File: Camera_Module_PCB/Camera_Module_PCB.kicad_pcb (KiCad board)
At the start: 4 copper layers, 111 parts, among them J1 SS-52400-002, J2 Conn_01x02, J3 FFC2A32-24-T, J4 U.FL-R-SMT-1_80_, SW1 SW_DIP_x01, SW2 SW_Push, SW3 SW_Push, U2 ESP32-S3R8, U4 MAX98357AETE_T, U5 AP3032KTR-G1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

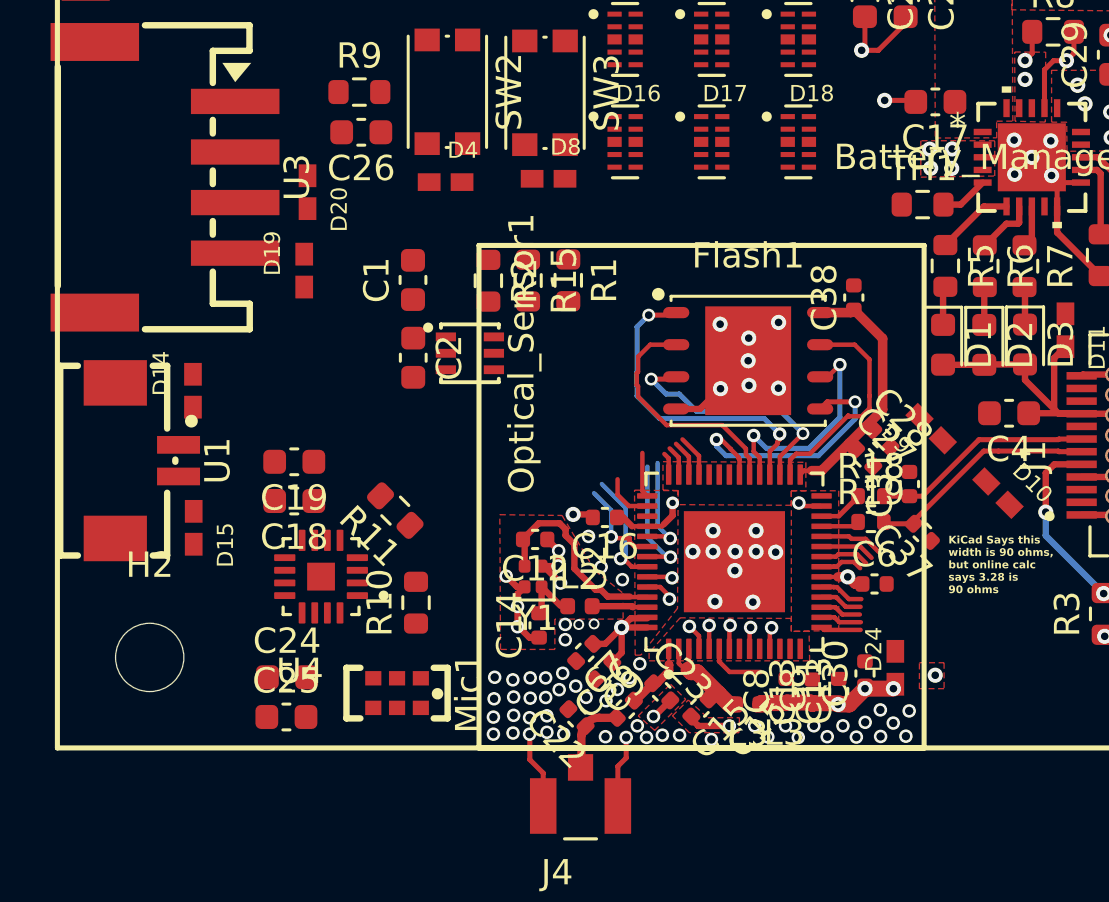
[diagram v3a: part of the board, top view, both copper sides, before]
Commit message: Began routing remaining paths
Routed the paths that connect the ESP32 chip and the amplifier IC that is used for the speaker. A large zone for the 3.3V power was created in the power plane to allow for power to be routed throughout the PCB.
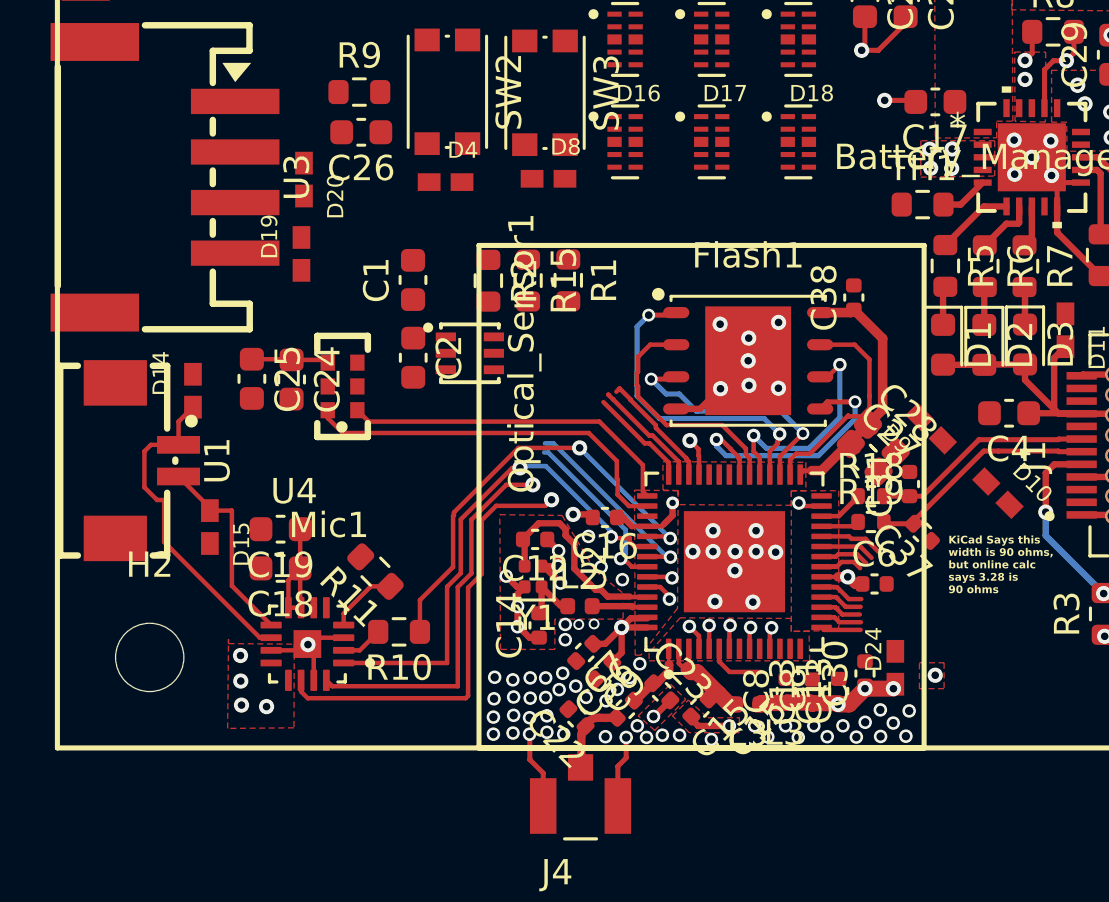
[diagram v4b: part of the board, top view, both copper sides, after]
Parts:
- C27, C28: footprint Capacitor_SMD:C_0402_1005Metric -> Capacitor_SMD:C_0603_1608Metric
- moved C25 13.4 mm to (109.3, 87.4), turned to -90 degrees
- moved Mic1 12.3 mm to (112.9, 87.7), turned to 180 degrees
- moved C24 11.8 mm to (110.9, 87.4), turned to -90 degrees
- moved C18 2.72 mm to (110.4, 94.9)
- moved C19 2.72 mm to (110.4, 93.4)
- moved U4 2.72 mm to (111.5, 97.9)
- moved R11 2.54 mm to (114.2, 95.0)
- moved R10 1.34 mm to (115.1, 97.4), turned to 180 degrees
- moved D19 0.67 mm to (111.2, 82.5)
- moved D15 0.64 mm to (107.6, 93.3)
- moved D20 0.52 mm to (111.3, 79.5)
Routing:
- net /LRCLK: track 7.11 -> 25.5 mm, vias 1 -> 2
- net /BCLK: track 6.51 -> 23.6 mm, vias 1 -> 2
- net /Din: track 3.68 -> 19.8 mm, vias 1 -> 2
- net /Gain: track 4.13 -> 17.3 mm, vias 1 -> 2
- net /PDM_DATA: track 1.97 -> 15.1 mm
- net Net-(U4-OUTN): track 0.00 -> 13.0 mm
- net /PDM_CLK: track 1.78 -> 13.5 mm
- net +3.3V: track 44.2 -> 52.6 mm
- net Net-(U4-OUTP): track 0.00 -> 7.89 mm
- net GND: track 50.9 -> 55.5 mm, vias 98 -> 103
- net /LED_CT: track 1.43 -> 4.72 mm
- net /SDA: track 1.18 -> 4.40 mm
- net /SCL: track 0.89 -> 4.05 mm
- net Net-(U2-U0TXD): track 4.96 -> 7.75 mm
- net Net-(U4-SD_MODE): track 0.00 -> 2.74 mm
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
